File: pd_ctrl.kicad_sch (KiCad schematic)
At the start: 1 part, among them U4 PD70100ILD-TR

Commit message: did stuff
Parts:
- renumbered U4 to U6
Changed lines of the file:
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@@
 		(dnp no)
 		(fields_autoplaced yes)
-		(property "Reference" "U4"
+		(property "Reference" "U6"
 			(at 142.24 66.04 0)
 			(effects
@@
 			(project ""
 				(path "/2970f661-65ab-4e2b-aeda-d76d1044f2b8/dfd7c564-50b6-4b87-afcf-cfbf80807611"
-					(reference "U4")
+					(reference "U6")
 					(unit 1)
 				)

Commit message: stuff
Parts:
- removed U6: PD70100ILD-TR, PD70100ILD-TR:DFN12_4X3_MCH, symbol PD70100ILD-TR:PD70100ILD-TR
- added U6: MP8030GQJ-P, QFN-32_MP8030_MNP, symbol MP8030GQJ-P:MP8030GQJ-P
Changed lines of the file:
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@@
 	(paper "A4")
 	(symbol
-		(lib_id "PD70100ILD-TR:PD70100ILD-TR")
-		(at 116.84 78.74 0)
+		(lib_id "MP8030GQJ-P:MP8030GQJ-P")
+		(at 59.69 83.82 0)
 		(unit 1)
 		(body_style 1)
@@
 		(fields_autoplaced yes)
 		(property "Reference" "U6"
-			(at 142.24 66.04 0)
+			(at 85.09 71.12 0)
 			(show_name no)
 			(do_not_autoplace no)
@@
 			)
 		)
-		(property "Value" "PD70100ILD-TR"
-			(at 142.24 68.58 0)
+		(property "Value" "MP8030GQJ-P"
+			(at 85.09 73.66 0)
 			(show_name no)
 			(do_not_autoplace no)
@@
 			)
 		)
-		(property "Footprint" "PD70100ILD-TR:DFN12_4X3_MCH"
-			(at 116.84 78.74 0)
+		(property "Footprint" "QFN-32_MP8030_MNP"
+			(at 59.69 83.82 0)
 			(hide yes)
 			(show_name no)
@@
 			)
 		)
-		(property "Datasheet" "PD70100ILD-TR"
-			(at 116.84 78.74 0)
+		(property "Datasheet" "https://www.monolithicpower.com/en/documentview/productdocument/index/version/2/document_type/Datasheet/lang/en/sku/MP8030GQJ"
+			(at 59.69 83.82 0)
 			(hide yes)
 			(show_name no)
@@
 		)
 		(property "Description" ""
-			(at 116.84 78.74 0)
+			(at 59.69 83.82 0)
 			(hide yes)
 			(show_name no)
@@
 			)
 		)
-		(pin "3"
+		(pin "22"
 		)
-		(pin "10"
+		(pin "24"
+		)
+		(pin "28"
+		)
+		(pin "29"
+		)
+		(pin "31"
+		)
+		(pin "33"
+		)
+		(pin "32"
+		)
+		(pin "1"
+		)
+		(pin "4"
 		)
 		(pin "11"
 		)
-		(pin "4"
+		(pin "14"
 		)
-		(pin "5"
+		(pin "17"
 		)
-		(pin "13"
+		(pin "18"
 		)
-		(pin "12"
+		(pin "6"
 		)
 		(pin "7"
@@
 		(pin "8"
 		)
-		(pin "6"
-		)
 		(pin "9"
 		)
-		(pin "1"
+		(pin "10"
+		)
+		(pin "12"
+		)
+		(pin "13"
+		)
+		(pin "15"
+		)
+		(pin "16"
+		)
+		(pin "19"
+		)
+		(pin "20"
+		)
+		(pin "21"
+		)
+		(pin "23"
+		)
+		(pin "25"
+		)
+		(pin "26"
+		)
+		(pin "27"
+		)
+		(pin "30"
 		)
 		(pin "2"
 		)
+		(pin "3"
+		)
+		(pin "5"
+		)
 		(instances

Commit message: lots
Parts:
- removed U6: MP8030GQJ-P, QFN-32_MP8030_MNP, symbol MP8030GQJ-P:MP8030GQJ-P
- added C135: 100n 100V, Capacitor_SMD:C_0603_1608Metric, symbol Device:C
- added C136: 4.7u, Capacitor_SMD:C_0805_2012Metric, symbol Device:C
- added R100: 240k, Resistor_SMD:R_0402_1005Metric, symbol Device:R
- added R101: 133, Resistor_SMD:R_0402_1005Metric, symbol Device:R
- added R102: 24.9k, Resistor_SMD:R_0402_1005Metric, symbol Device:R
- added U12: PD70100ILD-TR, PD70100ILD-TR:DFN12_4X3_MCH, symbol PD70100ILD-TR:PD70100ILD-TR
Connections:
- new net: R100.1, U12.2 (RREF)
- new net: R102.2, U12.1 (RDET)
- new net: R101.1, U12.3 (RCLASS)
- new net PD_AUX: C136.1, U12.11 (VAUX)
- new net PGND: C136.2, U12.7 (VPNOUT), U12.8 (VPNOUT)
- new net POE_V+: C135.1, R102.1, U12.12 (VPP)
- new net VIN-: C135.2, R100.2, R101.2, U12.13 (VPNIN), U12.4 (VPNIN), U12.5 (VPNIN)

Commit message: many stuffs
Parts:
- added TP181: TestPoint, TestPoint:TestPoint_THTPad_D1.0mm_Drill0.5mm, symbol Connector:TestPoint
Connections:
- net VIN-: now also TP181.1
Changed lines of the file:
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@@
+	)
+	(junction
+		(at 154.94 148.59)
+		(diameter 0)
+		(color 0 0 0 0)
 	)
 	(junction
@@
 	(wire
 		(pts
+			(xy 154.94 148.59) (xy 166.37 148.59)
+		)
+		(stroke
+			(width 0)
+			(type default)
+		)
+	)
+	(wire
+		(pts
 			(xy 166.37 125.73) (xy 166.37 135.89)
 		)
@@
 	(wire
 		(pts
-			(xy 149.86 148.59) (xy 166.37 148.59)
+			(xy 149.86 148.59) (xy 154.94 148.59)
 		)
 		(stroke
@@
 					(unit 1)
 				)
+			)
+		)
+	)
+	(symbol
+		(lib_id "Connector:TestPoint")
+		(at 154.94 148.59 0)
+		(mirror y)
+		(unit 1)
+		(body_style 1)
+		(exclude_from_sim no)
+		(in_bom yes)
+		(on_board yes)
+		(in_pos_files yes)
+		(dnp no)
+		(fields_autoplaced yes)
+		(property "Reference" "TP181"
+			(at 157.48 145.2879 0)
+			(show_name no)
+			(do_not_autoplace no)
+			(effects
+				(font
+					(size 1.27 1.27)
+				)
+				(justify right)
+			)
+		)
+		(property "Value" "TestPoint"
+			(at 153.6701 143.51 90)
+			(hide yes)
+			(show_name no)
+			(do_not_autoplace no)
+			(effects
+				(font
+					(size 1.27 1.27)
+				)
+				(justify left)
+			)
+		)
+		(property "Footprint" "TestPoint:TestPoint_THTPad_D1.0mm_Drill0.5mm"
+			(at 149.86 148.59 0)
+			(hide yes)
+			(show_name no)
+			(do_not_autoplace no)
+			(effects
+				(font
+					(size 1.27 1.27)
+				)
+			)
+		)
+		(property "Datasheet" ""
+			(at 149.86 148.59 0)
+			(hide yes)
+			(show_name no)
+			(do_not_autoplace no)
+			(effects
+				(font
+					(size 1.27 1.27)
+				)
+			)
+		)
+		(property "Description" "test point"
+			(at 154.94 148.59 0)
+			(hide yes)
+			(show_name no)
+			(do_not_autoplace no)
+			(effects
+				(font
+					(size 1.27 1.27)
+				)
+			)
+		)
+		(pin "1"
+		)
+		(instances
+			(project "netdaq"
+				(path "/2970f661-65ab-4e2b-aeda-d76d1044f2b8/dfd7c564-50b6-4b87-afcf-cfbf80807611"
+					(reference "TP181")
+					(unit 1)
+				)

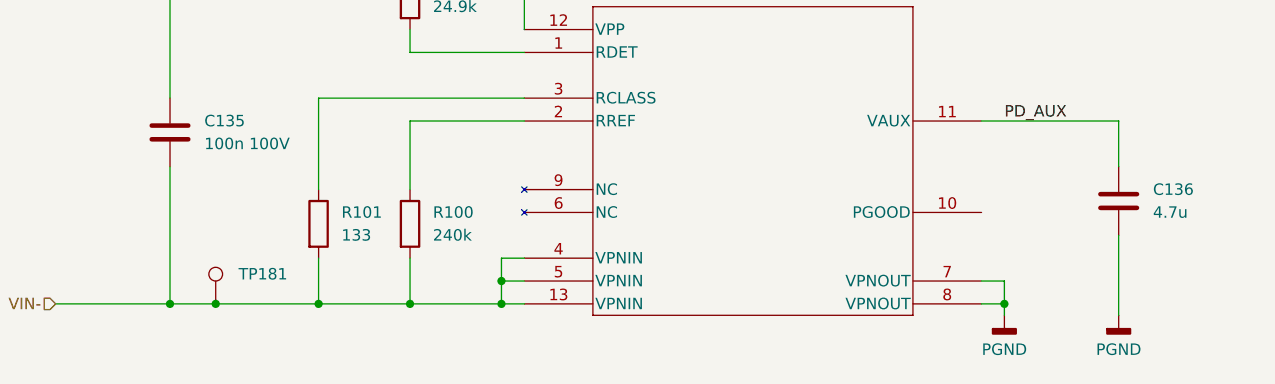
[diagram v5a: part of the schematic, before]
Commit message: did a bunch of bom matching to lcsc
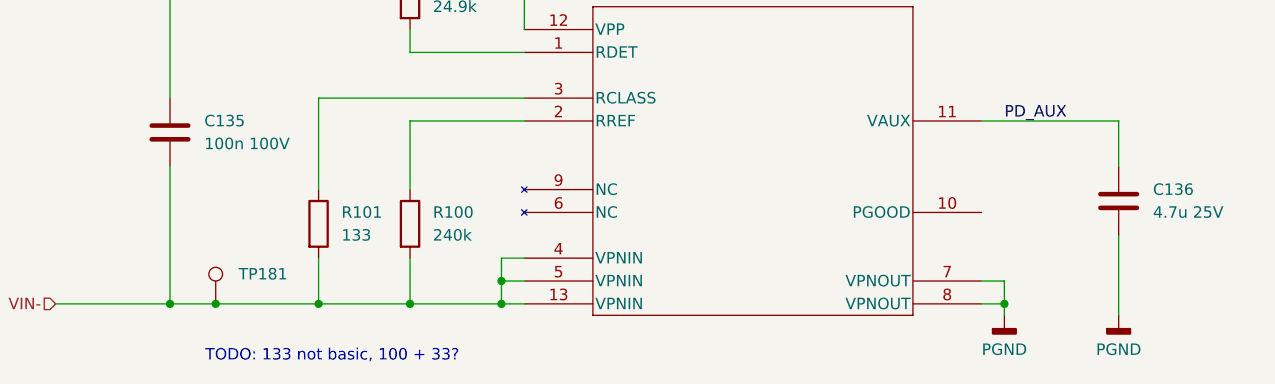
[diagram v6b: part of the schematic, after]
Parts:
- C135: footprint Capacitor_SMD:C_0603_1608Metric -> Capacitor_SMD:C_0805_2012Metric; LCSC (none) -> C28233; LCSC Basic/Pref (none) -> x; LCSC Part (none) -> C28233
- C136: value 4.7u -> 4.7u 25V; LCSC (none) -> C1779; LCSC Basic/Pref (none) -> x; LCSC Part (none) -> C1779
- R100: footprint Resistor_SMD:R_0402_1005Metric -> Resistor_SMD:R_0603_1608Metric; LCSC (none) -> C4197; LCSC Basic/Pref (none) -> x; LCSC Part (none) -> C4197
- R101, R102: LCSC Basic/Pref (none) -> n
- TP181: now left out of the parts list
- U12: LCSC Part (none) -> C5237659
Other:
- note added: "TODO: 133 not basic, 100 + 33?"

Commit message: bunch of stuff
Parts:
- added R108: 33, Resistor_SMD:R_0402_1005Metric, symbol Device:R
- added R109: 33k, Resistor_SMD:R_0402_1005Metric, symbol Device:R
- R101: value 133 -> 100; LCSC (none) -> C25076; LCSC Basic/Pref n -> x; LCSC Part (none) -> C25076
- R102: value 24.9k -> 100k; LCSC (none) -> C25741; LCSC Basic/Pref n -> y; LCSC Part (none) -> C25741
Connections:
- net POE_V+: now also R109.1
- net at R102.2, U12.1 (RDET): now also R109.2
- net at U12.3 (RCLASS): now also R108.1; no longer R101.1
- new net: R101.1, R108.2
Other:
- note removed: "TODO: 133 not basic, 100 + 33?"
